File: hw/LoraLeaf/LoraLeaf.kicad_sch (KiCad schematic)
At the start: 26 parts, among them U1 STM32WLE5CBUx, Y1 32.768KHz, Y2 32Mhz

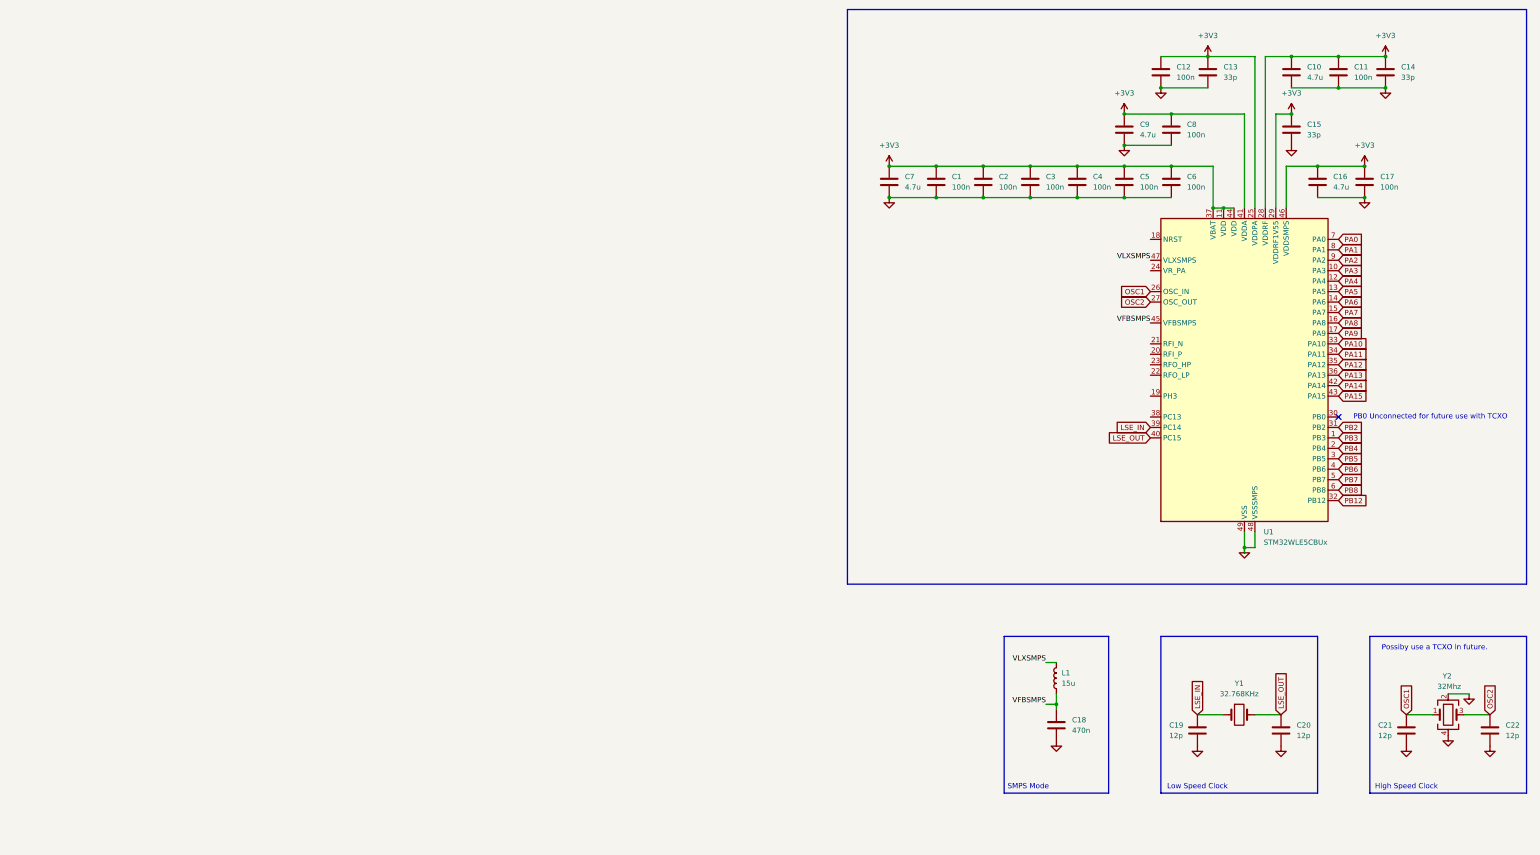
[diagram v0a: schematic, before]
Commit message: hw: sch: Added RF Section, remainder of MCU bringup, broken out power domains
Designed the RF Section (Balun, RF Switch, Antenna, and their respective
matching networks). In addition added remaining items for MCU bringup
such as clock, also fixed power to define different power domains.
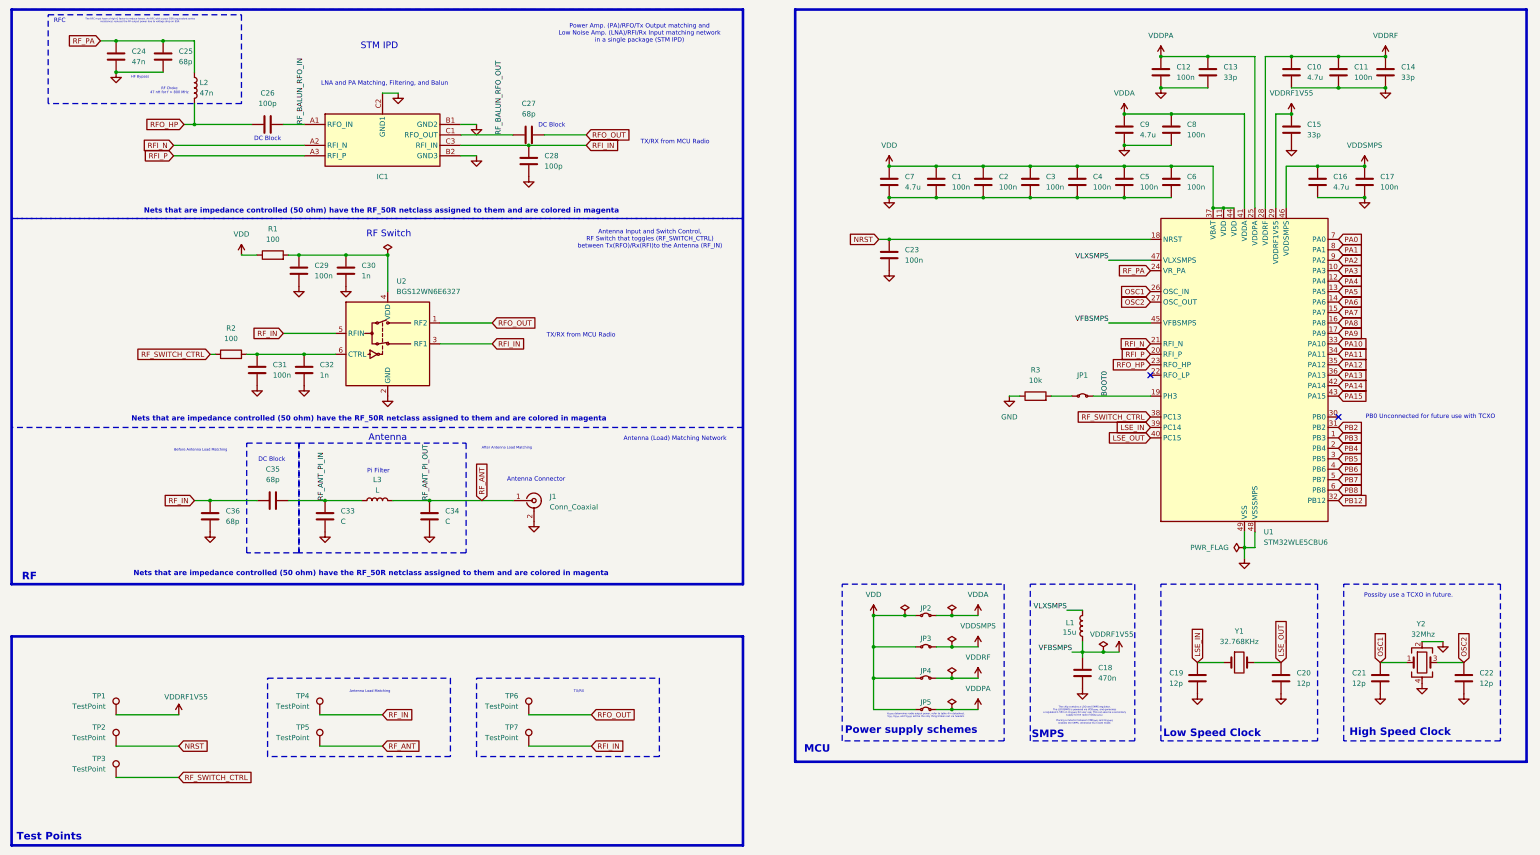
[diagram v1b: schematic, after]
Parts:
- added C23, C29, C31: 100n, Capacitor_SMD:C_0603_1608Metric, symbol Device:C
- added C24: 47n, Capacitor_SMD:C_0603_1608Metric, symbol Device:C
- added C25, C27, C35, C36: 68p, Capacitor_SMD:C_0402_1005Metric, symbol Device:C
- added C26, C28: 100p, Capacitor_SMD:C_0603_1608Metric, symbol Device:C
- added C30, C32: 1n, Capacitor_SMD:C_0603_1608Metric, symbol Device:C
- added C33, C34: C, symbol Device:C
- added IC1: ~, BALFHB-WL-02D3:BALFHBWL02D3, symbol BALFHB-WL-02D3:BALFHB-WL-02D3
- added J1: Conn_Coaxial, Connector_Coaxial:SMA_Amphenol_132134-10_Vertical, symbol Connector:Conn_Coaxial
- added JP1, JP2, JP3, JP4, JP5: Jumper_2_Small_Bridged, TestPoint:TestPoint_2Pads_Pitch2.54mm_Drill0.8mm, symbol Jumper:Jumper_2_Small_Bridged
- added L2: 47n, symbol Device:L
- added L3: L, symbol Device:L
- added R1, R2: 100, symbol Device:R
- added R3: 10k, symbol Device:R
- added TP1, TP2, TP3: TestPoint, TestPoint:TestPoint_Pad_1.0x1.0mm, symbol Connector:TestPoint
- added TP4, TP5, TP6, TP7: TestPoint, TestPoint:TestPoint_Loop_D1.80mm_Drill1.0mm_Beaded, symbol Connector:TestPoint
- added U2: BGS12WN6E6327, Package_LGA:Infineon_PG-TSNP-6-10_0.7x1.1mm_0.7x1.1mm_P0.4mm, symbol RF_Switch:BGS12WN6E6327
- C1, C10, C11, C12, C13, C14, C15, C16, C17, C18, C19, C2, C20, C21, C22, C3, C4, C5, C6, C7, C8, C9, Y1: JLC Part Type (none) -> Basic
- L1, Y2: JLC Part Type (none) -> Extended
- U1: value STM32WLE5CBUx -> STM32WLE5CBU6; JLC Part Type (none) -> Extended; MFR Part #  (none) -> STM32WLE5CBU6; Manafacturer (none) -> STMicroelectronics
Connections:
- net GND: now also C23.2, C24.2, C25.2, C28.1, C29.2, C30.2, C31.2, C32.2, C33.2, C34.2, C36.1, IC1.B1 (GND2), IC1.B2 (GND3), IC1.C2 (GND1), J1.2 (Ext), R3.1, U2.2 (GND)
- net NRST: now reaches U1.18 (NRST)
- net NRST: now also C23.1, TP2.1
- net BOOT0: now reaches U1.19 (PH3)
- net BOOT0: now also JP1.2 (B)
- net RFI_P: now reaches U1.20 (RFI_P)
- net RFI_P: now also IC1.A3 (RFI_P)
- net RFI_N: now reaches U1.21 (RFI_N)
- net RFI_N: now also IC1.A2 (RFI_N)
- net RFO_HP: now reaches U1.23 (RFO_HP)
- net RFO_HP: now also C26.1, L2.2
- net RF_PA: now reaches U1.24 (VR_PA)
- net RF_PA: now also C24.1, C25.1, L2.1
- net RF_SWITCH_CTRL: now reaches U1.38 (PC13)
- net RF_SWITCH_CTRL: now also R2.1, TP3.1
- removed net +3V3: C1.1, C10.1, C11.1, C12.1, C13.1, C14.1, C15.1, C16.1, C17.1, C2.1, C3.1, C4.1, C5.1, C6.1, C7.1, C8.1, C9.1, U1.11 (VDD), U1.25 (VDDPA), U1.28 (VDDRF), U1.29 (VDDRF1V55), U1.37 (VBAT), U1.41 (VDDA), U1.44 (VDD), U1.46 (VDDSMPS)
- net VFBSMPS renamed VDDRF1V55
- net VDDRF1V55: now also C15.1, U1.29 (VDDRF1V55), TP1.1
- new net: C29.1, C30.1, R1.2, U2.4 (VDD)
- new net: C31.1, C32.1, R2.2, U2.6 (CTRL)
- new net: JP1.1 (A), R3.2
- new net RFI_IN: C28.2, IC1.C3 (RFI_IN), TP7.1, U2.3 (RF1)
- new net RFO_OUT: C27.2, TP6.1, U2.1 (RF2)
- new net RF_ANT: C34.1, J1.1 (In), L3.2, TP5.1
- new net RF_ANT_PI_IN: C33.1, C35.2, L3.1
- new net RF_BALUN_RFO_IN: C26.2, IC1.A1 (RFO_IN)
- new net RF_BALUN_RFO_OUT: C27.1, IC1.C1 (RFO_OUT)
- new net RF_IN: C35.1, C36.2, TP4.1, U2.5 (RFIN)
- new net VDD: C1.1, C2.1, C3.1, C4.1, C5.1, C6.1, C7.1, JP2.1 (A), JP3.1 (A), JP4.1 (A), JP5.1 (A), R1.1, U1.11 (VDD), U1.37 (VBAT), U1.44 (VDD)
- new net VDDA: C8.1, C9.1, JP2.2 (B), U1.41 (VDDA)
- new net VDDPA: C12.1, C13.1, JP5.2 (B), U1.25 (VDDPA)
- new net VDDRF: C10.1, C11.1, C14.1, JP4.2 (B), U1.28 (VDDRF)
- new net VDDSMPS: C16.1, C17.1, JP3.2 (B), U1.46 (VDDSMPS)
- no-connect marks 1 -> 2
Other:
- note added: "After Antenna Load Matching"
- note added: "Antenna"
- note added: "Antenna (Load) Matching Network"
- note added: "Antenna Connector"
- note added: "Antenna Input and Switch Control, RF Switch that toggles (RF_SWITCH_CTRL) between Tx(RFO)/Rx(RFI)to the Antenna (RF_IN)"
- note added: "Antenna Load Matching"
- note added: "Before Antenna Load Matching"
- note added: "DC Block"
- note added: "HF Bypass"
- note added: "LNA and PA Matching, Filtering, and Balun"
- note added: "MCU"
- note added: "Nets that are impedance controlled (50 ohm) have the RF_50R netclass assigned to them and are colored in magenta"
- note added: "Pi Filter"
- note added: "Power Amp. (PA)/RFO/Tx Output matching and Low Noise Amp. (LNA)/RFI/Rx Input matching network in a single package (STM IPD)"
- note added: "Power supply schemes"
- note added: "RF"
- note added: "RF Choke 47 nH for f > 800 MHz"
- note added: "RF Switch"
- note added: "RFC"
- note added: "SMPS"
- note added: "STM IPD"
- note added: "TX/RX"
- note added: "TX/RX from MCU Radio"
- note added: "Test Points"
- note added: "The RFC must have a high-Q factor to reduce losses. An RFC with a poor ESR (equivalent series resistance) reduces the RF output power due to voltage drop on ESR."
- note added: "The chip contains a LDO and SMPS regulator. The LDO/SMPS is powered via VDD_{SMPS}, and generates a regulated 1.55V on V_{FBSMPS} for user use. This can also be a secondary supply to the radio (VDD_{RF1V55}). Placing a inductor between VDD_{SMPS} and V_{FBSMPS} enables the SMPS, otherwise its in LDO mode."
- note added: "V_{DDPA} determines radio output power, refer to table 4 in datasheet. V_{DD}, V_{DDA}, and V_{DDRF} will be the only thing broken out via headers"
- note removed: "SMPS Mode"
- moved on the sheet: C18, C19, C20, C21, C22, L1, Y1, Y2
